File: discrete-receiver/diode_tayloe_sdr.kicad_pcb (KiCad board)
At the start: 4 copper layers, 110 x 110 mm, 268 parts, among them J2 Optional 5V DC Jack, J3 External Filter, J4 Debug Pins, J5 Display Connector, J6 SI-52003-F, T1 H1102NLT, T2 MABA-007159-000000, U1 SN74CBT3253DBQR, U10 MS5351M, U11 Ag9905LP, U13 LM66100DCK, U14 LM66100DCK, U15 LM66100DCK, U16 PSA4-5043_, U2 OPA1612AxD, U3 OPA1612AxD, U4 CJC5340, U5 ADE-1+, U6 RP2350A, U7 W25Q128, U9 LAN8720A, X1 YC24.576MUBCE2O, X2 X322512MSB4SI

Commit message: PCB has begun.
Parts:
- removed C105: 100nF, PCM_JLCPCB:C_0402
- removed C106: 100pF, PCM_JLCPCB:C_0603
- added C69: 100nF, PCM_JLCPCB:C_0402, F.Cu at (72.1, 135.0)
- added C79: 100pF, PCM_JLCPCB:C_0603, F.Cu at (71.0, 134.5)
- L7: footprint Inductor_SMD:L_APV_AHW2520 -> sdr_project:L_APV_AHW2520
- OLED Display: renamed from J5
- R8, R9: value 47Ω -> 27Ω; footprint PCM_JLCPCB:R_0402 -> PCM_JLCPCB:R_0603
- SWD Debug: renamed from J4
- moved C101 253.2 mm to (92.3, 250.0), turned to -90 degrees
- moved C103 252.5 mm to (91.2, 250.0), turned to -90 degrees
- moved JP15 248.9 mm to (66.5, 249.7), turned to 90 degrees
- moved D11 243.2 mm to (76.6, 263.9), turned to 180 degrees
- moved JP16 242.8 mm to (84.2, 262.4)
- moved D12 239.0 mm to (76.6, 261.5)
- moved JP2 238.4 mm to (8.34, 115.0), turned to -90 degrees
- moved JP17 236.7 mm to (89.9, 263.0), turned to 180 degrees
- moved JP5 232.5 mm to (37.4, 44.5)
- moved C108 228.6 mm to (-17.9, 100.3), turned to 180 degrees
- moved J3 226.1 mm to (35.0, 119.1), turned to 180 degrees
- moved T1 221.5 mm to (84.0, 252.5), turned to 90 degrees
- moved C107 220.4 mm to (-17.8, 99.2), turned to 180 degrees
- moved U5 216.3 mm to (44.4, 119.2), turned to -90 degrees
- moved C97 216.1 mm to (47.4, 113.7), turned to 180 degrees
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- renumbered TP17 to POE+, TP18 to POE-, TP16 to POE_Raw
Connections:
- R8 pad 1: Net-(U6-USB_DM) -> Net-(U6-USB_DP)
- R8 pad 2: /Pico/Pico_USB- -> /Pico/Pico_USB+
- R9 pad 1: Net-(U6-USB_DP) -> Net-(U6-USB_DM)
- R9 pad 2: /Pico/Pico_USB+ -> /Pico/Pico_USB-
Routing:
- net Net-(J3-Pin_1): track 0.00 -> 39.7 mm
- net +2.4V_A: track 0.00 -> 37.4 mm
- net Net-(JP2-A): track 0.00 -> 33.9 mm
- net Net-(J3-Pin_4): track 0.00 -> 20.7 mm
- net VHF IF: track 0.00 -> 18.4 mm
- net Net-(C61-Pad2): track 0.00 -> 17.4 mm
- net Net-(D10-Pad2): track 0.00 -> 17.0 mm
- net QSPI_SS: track 0.00 -> 16.0 mm
- net QSPI_SD1: track 0.00 -> 14.9 mm
- net HF: track 0.00 -> 14.5 mm
- net /Receiver/Charles/RF In: track 0.00 -> 13.0 mm
- net Net-(C6-Pad1): track 0.00 -> 11.2 mm
- net QSPI_SD2: track 0.00 -> 10.8 mm
- net Net-(C62-Pad2): track 0.00 -> 7.79 mm
- net QSPI_SD3: track 0.00 -> 7.76 mm
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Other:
- board text added: "GPIO26"
- board text added: "GPIO29"
- board text added: "GPIO4"
- board text added: "GPIO5"
- board text added: "Power"
- board text added: "This is the H1102NLT transfomer + tayloe detector + ADC It was setup one way, but now it needs to be setup another after the RF filtering + etc. was redrawn."

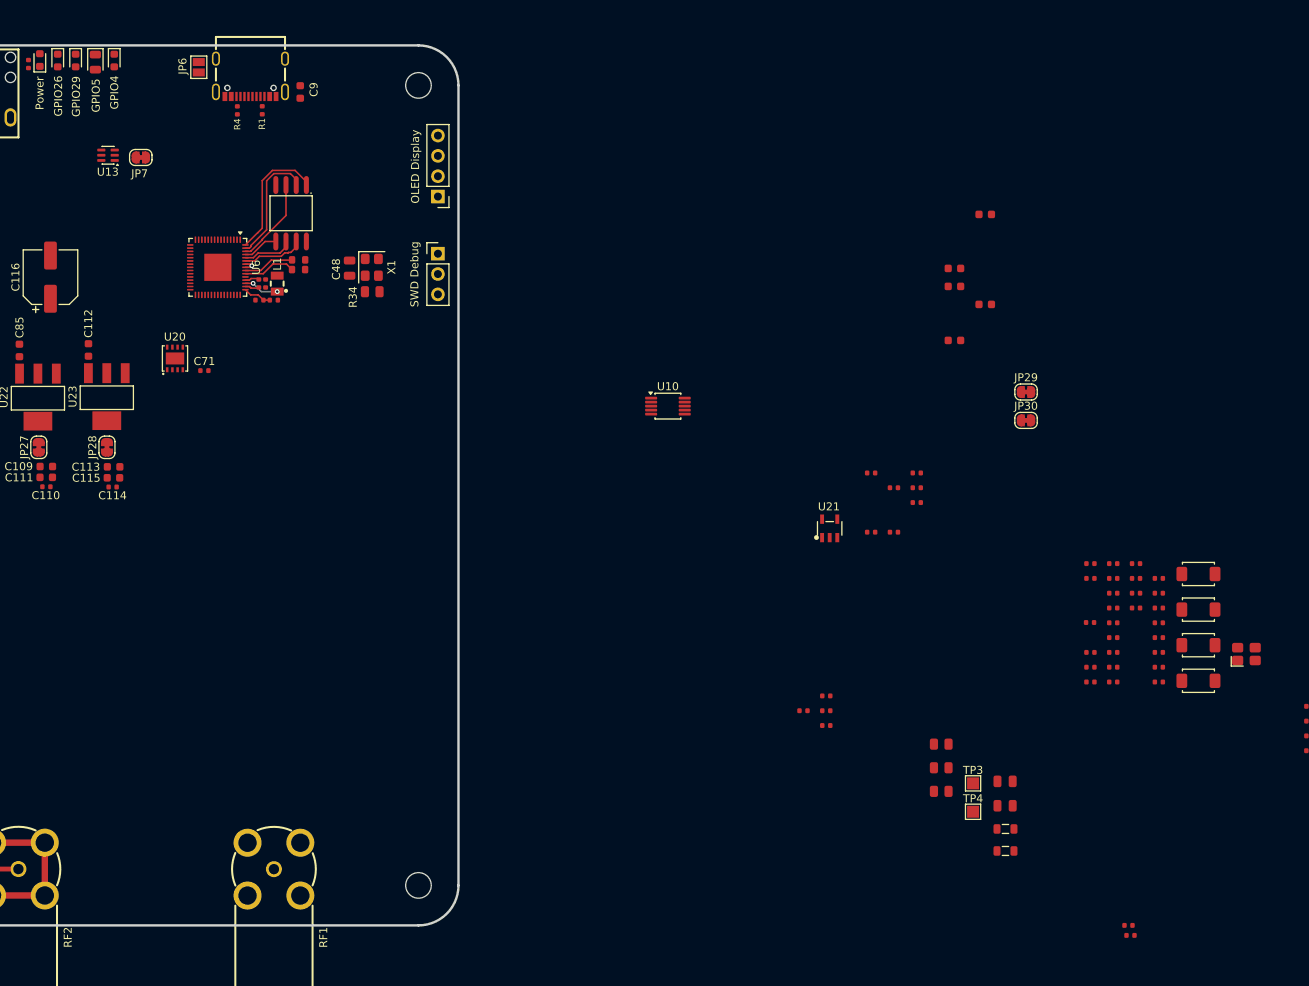
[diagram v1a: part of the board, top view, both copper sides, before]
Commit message: PCB Layout update
buttons, LED/Resistors, Collection of Clock Gen components
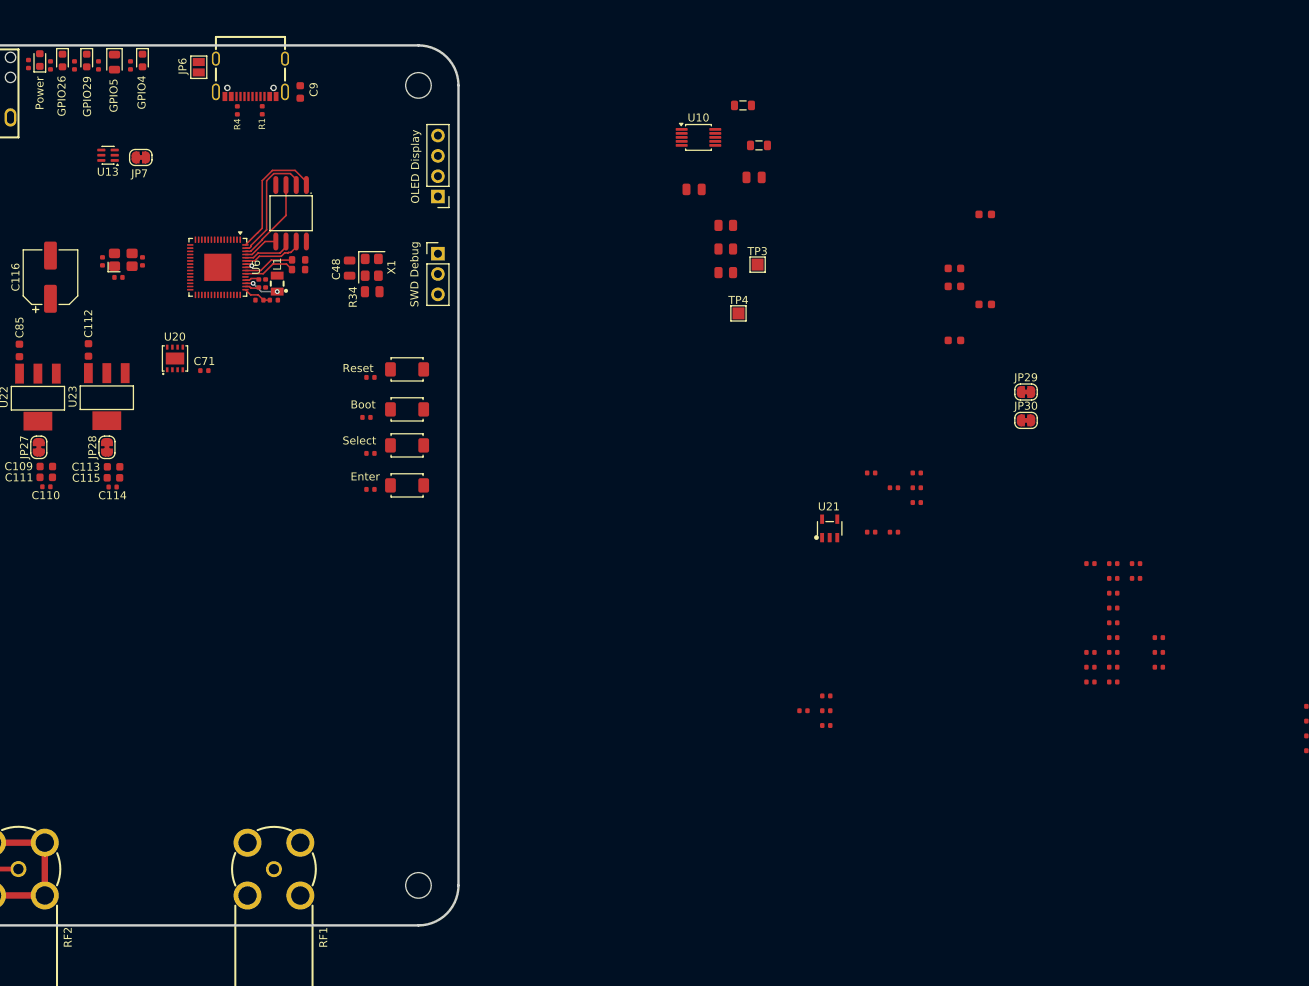
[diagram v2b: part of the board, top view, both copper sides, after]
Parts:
- moved R12 167.7 mm to (97.5, 34.0), turned to 90 degrees
- moved R11 165.7 mm to (101.5, 34.0), turned to 90 degrees
- moved R39 158.5 mm to (91.5, 34.0), turned to 90 degrees
- moved R19 151.6 mm to (94.5, 34.0), turned to 90 degrees
- moved X2 148.8 mm to (100.6, 58.3)
- moved R5 133.2 mm to (100.0, 60.5)
- moved C17 131.4 mm to (98.0, 58.5), turned to -90 degrees
- moved C14 124.9 mm to (103.0, 58.5), turned to 90 degrees
- moved S4 104.6 mm to (136.1, 77.0), turned to 180 degrees
- moved R22 102.3 mm to (131.0, 78.0)
- moved S1 102.2 mm to (136.1, 72.0), turned to 180 degrees
- moved S2 101.0 mm to (136.1, 81.5), turned to 180 degrees
- moved S3 100.9 mm to (136.1, 86.5), turned to 180 degrees
- moved R6 99.9 mm to (131.5, 73.0)
- moved R16 99.8 mm to (131.5, 82.5)
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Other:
- board text added: "Boot"
- board text added: "Enter"
- board text added: "Reset"
- board text added: "Select"

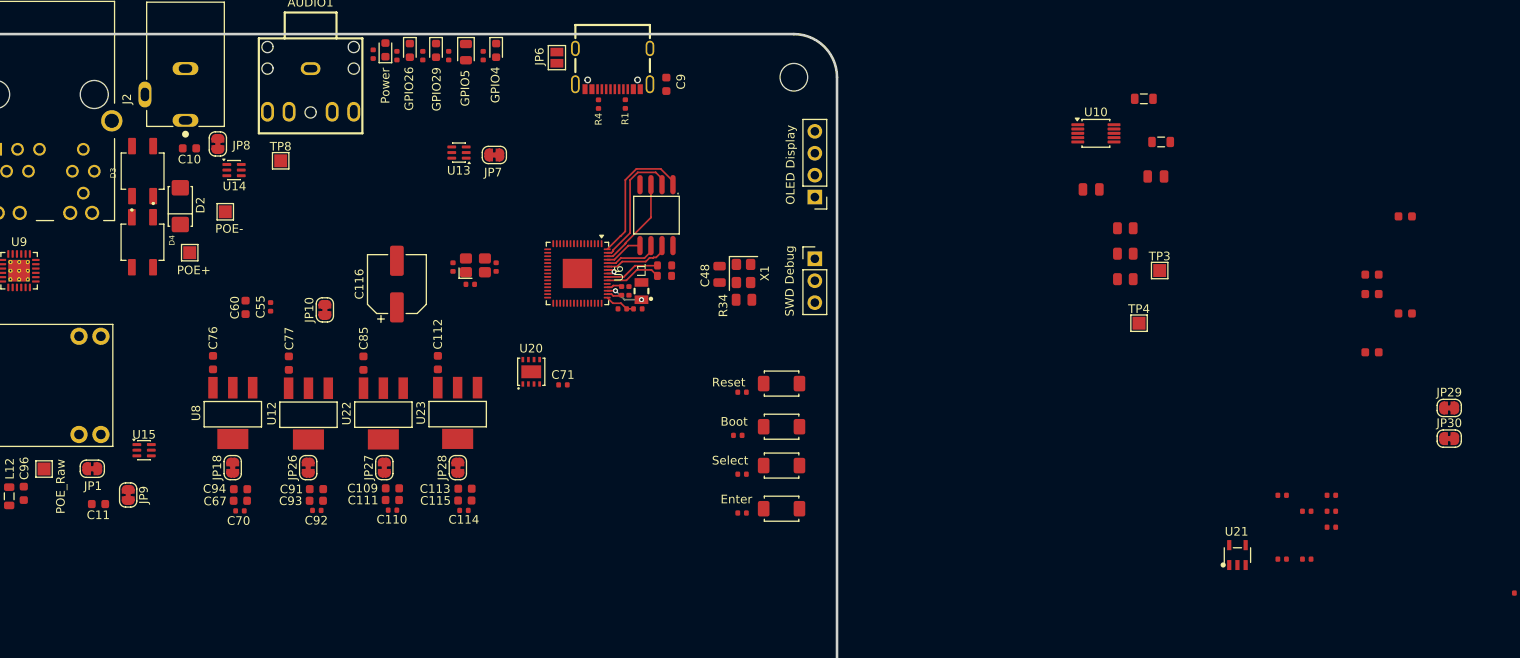
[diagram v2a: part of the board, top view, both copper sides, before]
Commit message: Add missing Jumper foot print, continue organising components
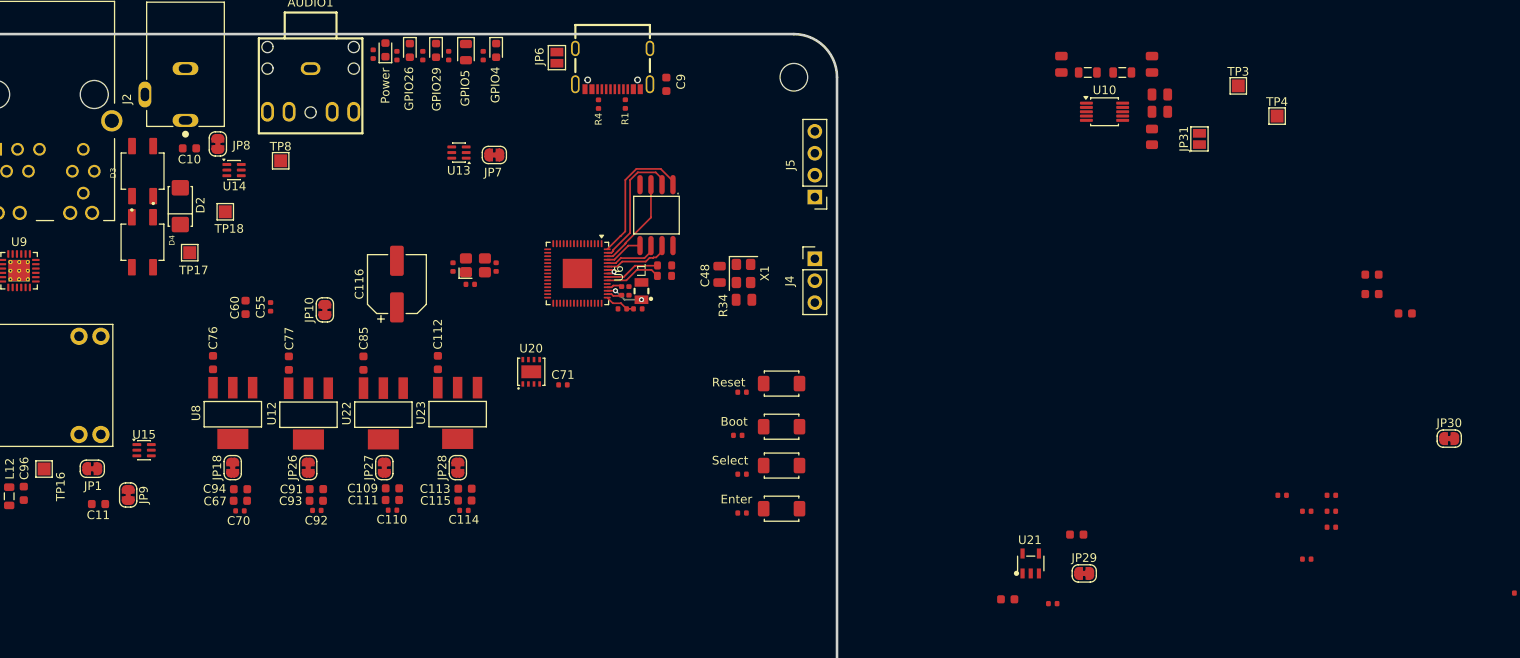
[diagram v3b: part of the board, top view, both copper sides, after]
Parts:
- added JP31: SolderJumper_2_Open, Jumper:SolderJumper-2_P1.3mm_Open_Pad1.0x1.5mm, F.Cu at (184.5, 43.6)
- J4: renamed from SWD Debug
- J5: renamed from OLED Display
- moved C75 53.0 mm to (170.3, 89.5)
- moved C73 51.0 mm to (162.3, 97.0)
- moved JP29 46.4 mm to (171.2, 94.0)
- moved TP4 28.8 mm to (193.5, 41.0)
- moved C74 27.1 mm to (167.5, 97.5)
- moved U21 24.0 mm to (164.9, 92.8)
- moved TP3 23.3 mm to (189.0, 37.5)
- moved R38 16.9 mm to (179.9, 40.5)
- moved R42 16.8 mm to (179.0, 43.4), turned to 90 degrees
- moved R37 16.0 mm to (179.9, 38.5), turned to 180 degrees
- moved C46 14.9 mm to (168.5, 35.0), turned to -90 degrees
- moved C47 13.0 mm to (179.0, 35.0), turned to -90 degrees
- moved FB2 9.22 mm to (175.6, 36.0)
- moved FB4 7.18 mm to (171.6, 36.0)
- moved U10 2.69 mm to (173.5, 40.5)
- renumbered POE_Raw to TP16, POE+ to TP17, POE- to TP18
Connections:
- net ADC out SCLK renamed /ADC/I2S_SCLK
- net ADC out SD renamed /ADC/I2S_SD
- net ADC out WS renamed /ADC/I2S_WS

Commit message: Progress on PCB
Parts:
- JP5, JP8, TP17, TP18, TP8, U11: moved to B.Cu
- moved R32 218.7 mm to (45.6, 53.8), turned to 180 degrees
- moved R31 216.4 mm to (47.4, 53.8)
- moved R33 211.3 mm to (54.0, 53.8), turned to 180 degrees
- moved R30 207.9 mm to (55.8, 53.8)
- moved U11 37.0 mm to (74.3, 68.2)
- moved C112 22.3 mm to (110.2, 87.0)
- moved C76 22.3 mm to (84.1, 87.0)
- moved C93 22.3 mm to (96.1, 103.0)
- moved C94 22.3 mm to (87.3, 101.7)
- moved C111 22.3 mm to (104.9, 103.0)
- moved C115 22.3 mm to (113.3, 103.0)
- moved C67 22.3 mm to (87.3, 103.0)
- moved C77 22.3 mm to (92.9, 87.1)
- moved C85 22.3 mm to (101.5, 87.1)
- moved JP18 22.3 mm to (86.4, 99.2)
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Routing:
- net POE -: track 0.00 -> 19.3 mm
- net POE +: track 0.00 -> 17.7 mm
- net Net-(J6-SHIELD): track 0.00 -> 15.5 mm
- net TX+: track 0.00 -> 14.1 mm, vias 0 -> 1
- net POE B1: track 0.00 -> 14.0 mm, vias 0 -> 1
- net TX-: track 0.00 -> 12.1 mm, vias 0 -> 1
- net GND: track 1.79 -> 13.9 mm
- net POE B2: track 0.00 -> 11.0 mm, vias 0 -> 1
- net RX-: track 0.00 -> 9.94 mm
- net Eth LED 1: track 0.00 -> 9.79 mm, vias 0 -> 2
- net POE A2: track 0.00 -> 9.60 mm
- net +3.3V: track 3.57 -> 12.9 mm
- net POE A1: track 0.00 -> 8.12 mm
- net RX+: track 0.00 -> 7.72 mm
- net Eth LED 2: track 0.00 -> 3.86 mm
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
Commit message: PCB Progress
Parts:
- moved R18 214.4 mm to (47.0, 54.6), turned to 180 degrees
- moved U14 5.62 mm to (67.0, 46.6)
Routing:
- net +3.3V: track 12.9 -> 23.8 mm, vias 1 -> 4
- net Net-(JP10-B): track 0.00 -> 4.65 mm, vias 0 -> 1
- net POE -: track 19.3 -> 21.3 mm
- net Net-(U9-RBIAS): track 0.00 -> 2.01 mm
- net POE +: track 17.7 -> 19.7 mm
- net Net-(JP8-A): track 0.00 -> 1.78 mm, vias 0 -> 1
- net GND: track 13.9 -> 15.6 mm
- net Eth LED 2: track 3.86 -> 4.40 mm, vias 0 -> 2

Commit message: PCB progress
POE design
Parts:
- removed C11: 10uF, PCM_JLCPCB:C_0603
- JP7: moved to B.Cu
- moved C72 31.5 mm to (66.5, 68.2)
- moved C78 30.5 mm to (71.8, 70.2)
- moved L12 30.4 mm to (73.2, 70.5)
- moved TP16 29.8 mm to (77.1, 68.2)
- moved C96 26.9 mm to (72.4, 72.8), turned to 180 degrees
- moved R9 18.4 mm to (117.0, 41.9), turned to 90 degrees
- moved R13 18.4 mm to (120.9, 45.0), turned to -90 degrees
- moved R8 17.7 mm to (115.8, 41.9), turned to 90 degrees
- moved C18 16.8 mm to (120.9, 46.8), turned to -90 degrees
- moved L1 16.7 mm to (118.8, 44.6), turned to 0 degrees
- moved JP9 15.8 mm to (72.4, 74.7), turned to 0 degrees
- moved JP1 15.3 mm to (56.9, 66.6), turned to 180 degrees
- moved C16 15.2 mm to (118.8, 46.0), turned to 0 degrees
- moved U7 15.1 mm to (110.0, 42.9), turned to -90 degrees
- moved C15 14.4 mm to (118.8, 46.9), turned to 0 degrees
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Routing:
- net +3.3V: track 23.8 -> 43.5 mm, vias 4 -> 8
- net Net-(JP6-A): track 0.00 -> 19.0 mm
- net /Power/USB 5V: track 0.00 -> 10.5 mm, vias 0 -> 3
- net Net-(C72-Pad1): track 0.00 -> 7.99 mm
- net +1.1V: track 0.00 -> 6.66 mm, vias 0 -> 2
- net Net-(JP10-B): track 4.65 -> 10.7 mm, vias 1 -> 3
- net /Pico/Pico_USB+: track 0.00 -> 5.93 mm
- net /Pico/Pico_USB-: track 0.00 -> 4.94 mm
- net POE_5.65V: track 0.00 -> 4.42 mm
- net GND: track 15.6 -> 18.6 mm
- net Net-(D13-Pad2): track 0.00 -> 1.95 mm
- net Net-(JP9-A): track 0.00 -> 1.87 mm
- net Net-(JP1-B): track 0.00 -> 1.83 mm
- net Net-(D7-Pad2): track 0.00 -> 1.61 mm
- net Net-(D5-Pad2): track 0.00 -> 1.58 mm
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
